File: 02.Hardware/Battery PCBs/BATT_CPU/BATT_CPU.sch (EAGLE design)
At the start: 68 parts, among them J1 2314820-6, K3 FLEX_CONN, K4 FLEX6, K5 FLEX8, U1 ATSAMD21G18_QFN, U2 TPS78230DDCR, U3 TPS78230DDCR, U4 TS3USB221A, U5 MAX9062EUK+T, U6 MAX9062EUK+T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

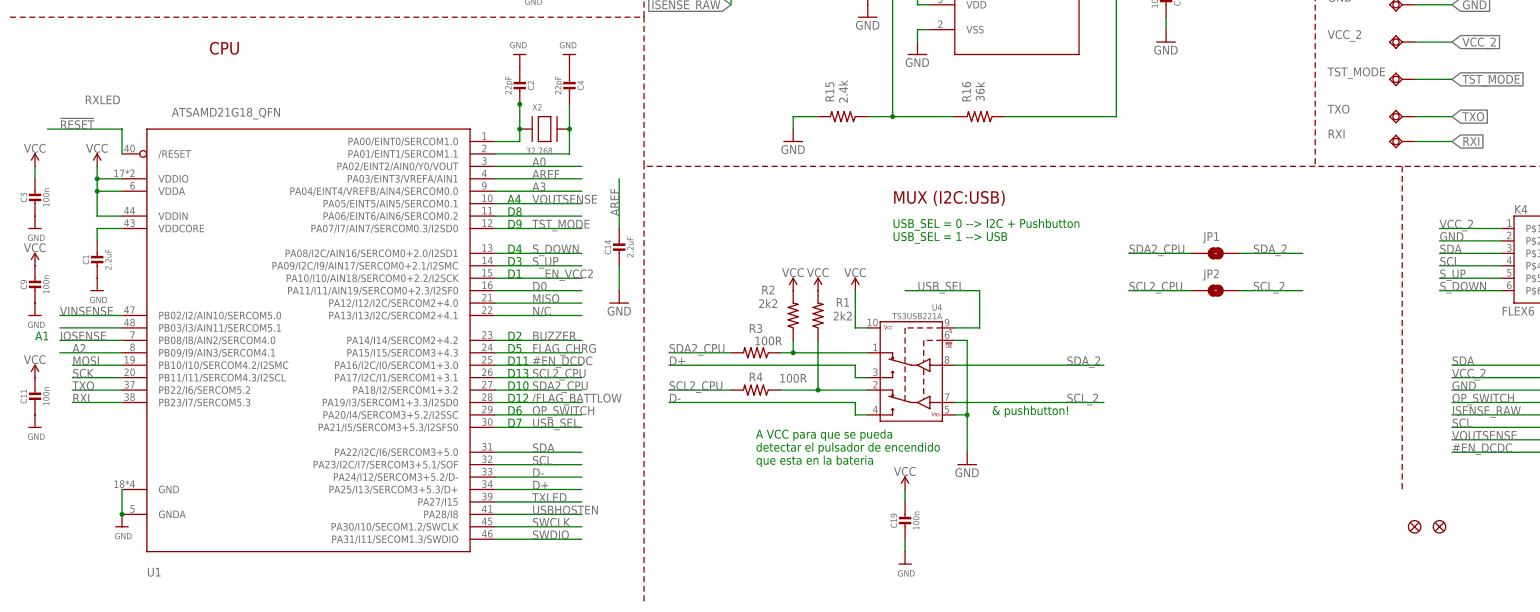
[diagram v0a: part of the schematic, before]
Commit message: Cambios revisados con David
Revision de los pcbs de la bateria.

En el DCDC se añade un diode Clamp (bat54s) en la medicion de la tension de salida.
Actualizacion de la BOM a v8.
Documentos de Cambios de versiones
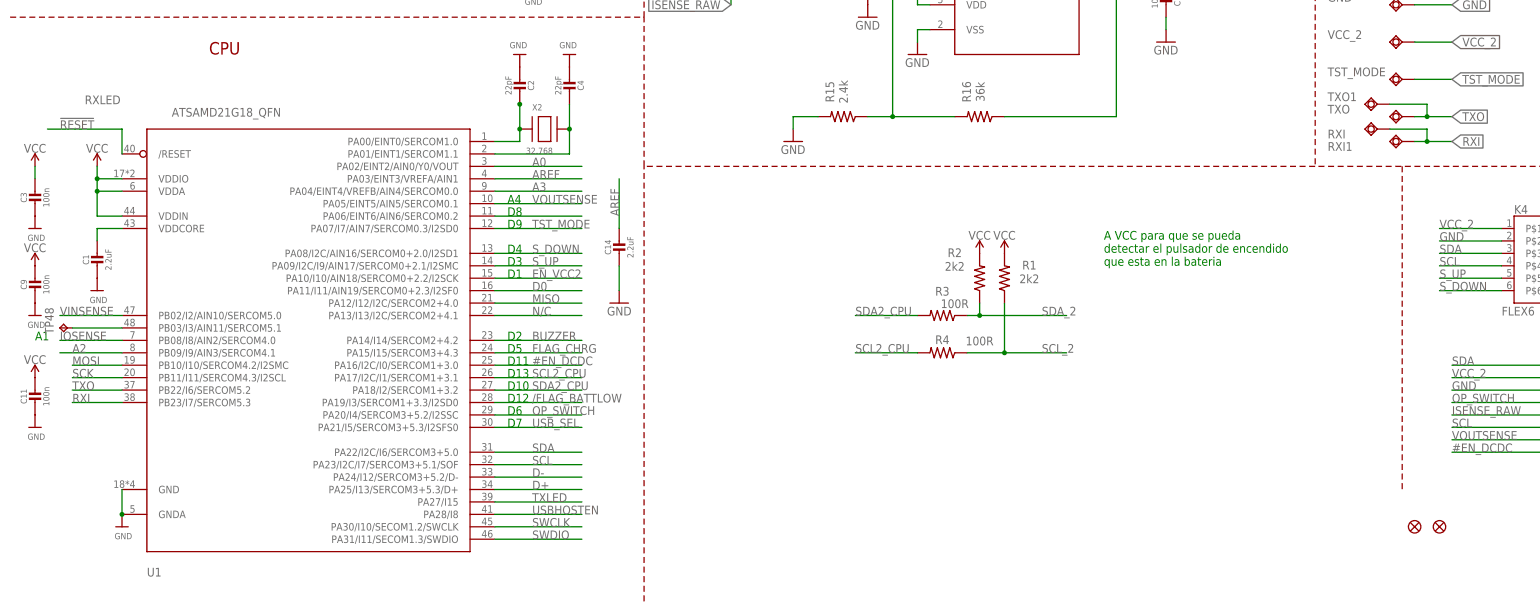
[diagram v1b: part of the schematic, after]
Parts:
- removed C19: 100n, microbuilder:CAP_CERAMIC0603_NO
- removed JP1, JP2: JUMPER-SMT_2_NO_SILK, SparkFun-Jumpers:JUMPER-SMT_2_NO_SILK
- removed U4: TS3USB221A, SparkFun-IC-Special-Function:TS3USB221A
- added RXI1, TXO1: TESTPAD_TPSQB1,27, BeagleBone_Blue_R3:TESTPAD_TPSQB1,27
- added TP48: TPTP08R, testpad:TPTP08R
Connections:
- removed net N$2: R2.1, R3.1, U4.1D+
- removed net N$3: R1.1, R4.1, U4.1D-
- net D+: no longer U4.2D+
- net D-: no longer U4.2D-
- net GND: no longer C19.2, U4.!OE, U4.VSS
- net N$15: now also TP48.TP
- net RXI: now also RXI1.TP
- net SCL2_CPU: no longer JP2.1
- net SCL_2: now also R1.1, R4.1; no longer JP2.2, U4.D-
- net SDA2_CPU: no longer JP1.1
- net SDA_2: now also R2.1, R3.1; no longer JP1.2, U4.D+
- net TXO: now also TXO1.TP
- net USB_SEL: no longer U4.S
- net VCC: no longer C19.1, U4.VCC
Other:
- note removed: "& pushbutton!"
- note removed: "MUX (I2C:USB)"
- note removed: "USB_SEL = 0 --> I2C + Pushbutton USB_SEL = 1 --> USB"
- moved on the sheet: R1, R2, R3, R4

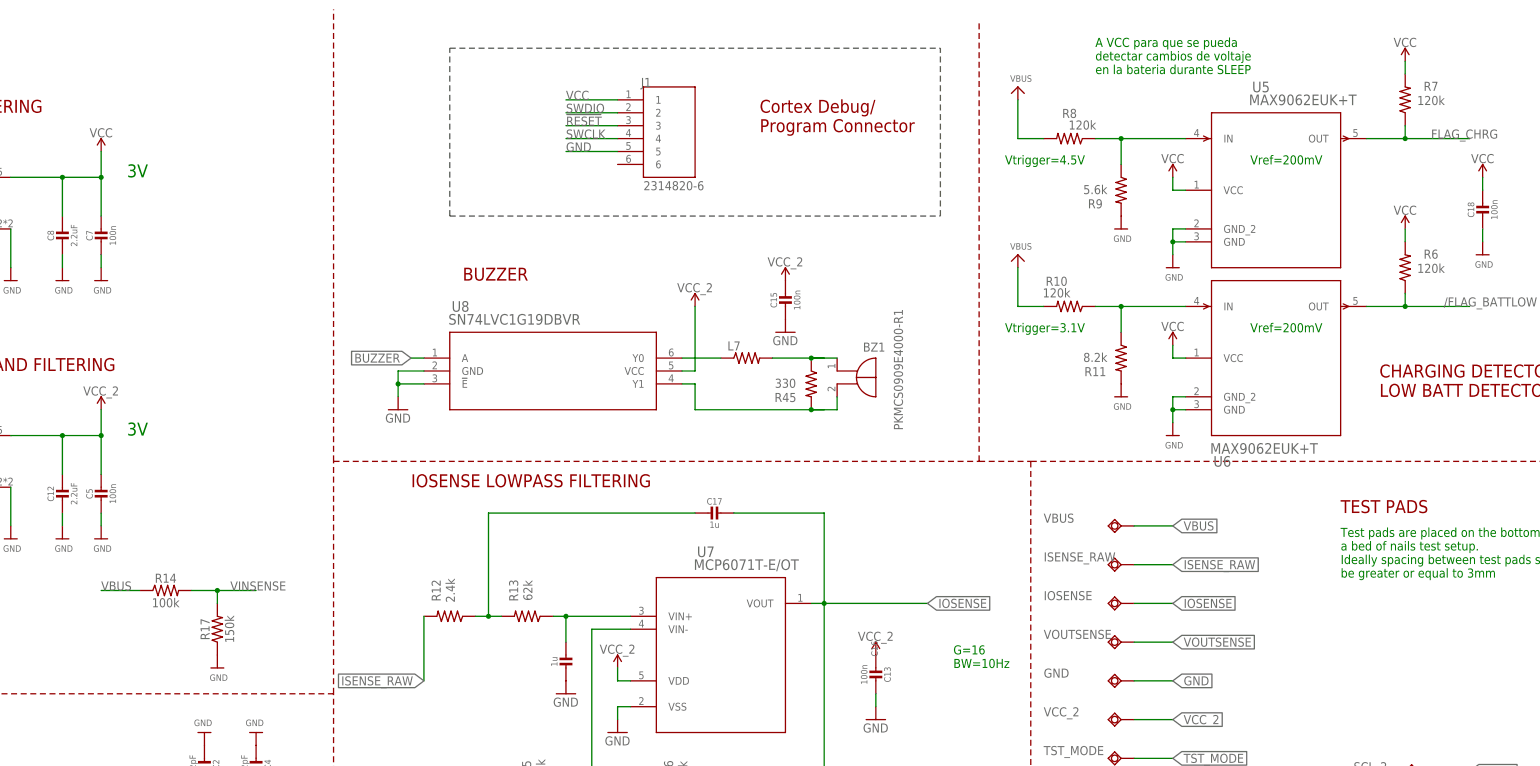
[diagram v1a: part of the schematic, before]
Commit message: Revision antes de Produccion
r6, r7: 120k a 10k
r45: no se monta
se añaden notas
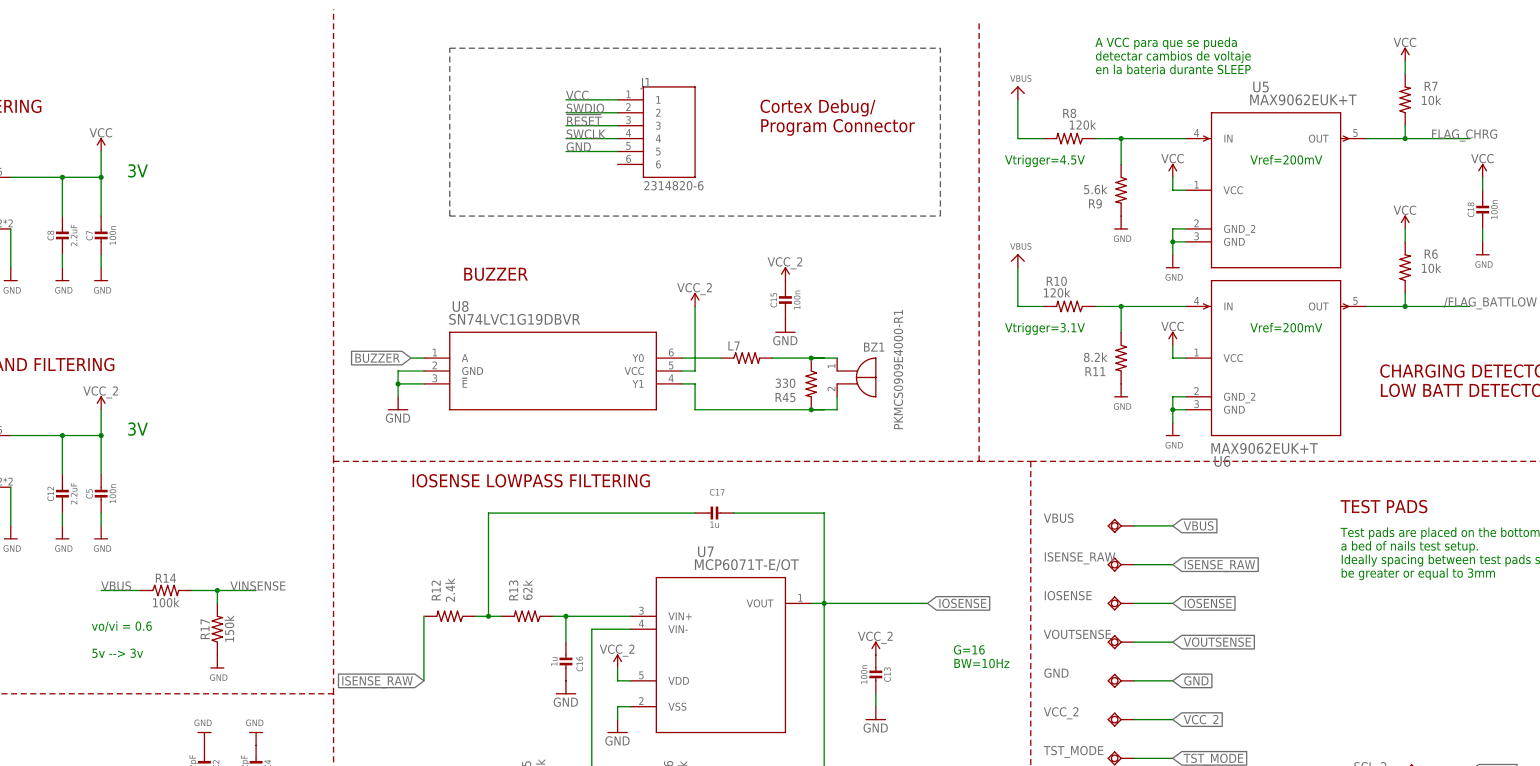
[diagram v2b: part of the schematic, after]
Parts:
- R6, R7: value 120k -> 10k
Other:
- note added: "vo/vi = 0.6 5v --> 3v"
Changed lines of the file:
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@@
 <setting verticaltext="up"/>
 </settings>
-<grid distance="0.1" unitdist="inch" unit="inch" style="lines" multiple="1" display="no" altdistance="0.01" altunitdist="inch" altunit="inch"/>
+<grid distance="1" unitdist="mm" unit="mm" style="lines" multiple="1" display="no" altdistance="0.01" altunitdist="inch" altunit="inch"/>
 <layers>
 <layer number="1" name="Top" color="4" fill="1" visible="no" active="no"/>
@@
 <part name="U5" library="MAX9062" deviceset="MAX9062EUK+T" device=""/>
 <part name="U6" library="MAX9062" deviceset="MAX9062EUK+T" device=""/>
-<part name="R6" library="SparkFun-Resistors" deviceset="RESISTOR" device="0603" value="120k"/>
-<part name="R7" library="SparkFun-Resistors" deviceset="RESISTOR" device="0603" value="120k"/>
+<part name="R6" library="SparkFun-Resistors" deviceset="RESISTOR" device="0603" value="10k"/>
+<part name="R7" library="SparkFun-Resistors" deviceset="RESISTOR" device="0603" value="10k"/>
 <part name="SUPPLY11" library="SparkFun-PowerSymbols" deviceset="VCC" device=""/>
 <part name="SUPPLY12" library="SparkFun-PowerSymbols" deviceset="VCC" device=""/>
@@
 <text x="106.68" y="81.28" size="1.778" layer="91">D8</text>
 <text x="106.68" y="78.74" size="1.778" layer="91">D9</text>
+<text x="87" y="129" size="1.778" layer="91">vo/vi = 0.6
+5v --&gt; 3v</text>
 </plain>
 <instances>
@@
 </instance>
 <instance part="C16" gate="G$1" x="180.34" y="127" smashed="yes" rot="MR0">
-<attribute name="NAME" x="241.05" y="130.79" size="1.27" layer="95" font="vector" rot="MR90" align="center"/>
+<attribute name="NAME" x="183.05" y="127.79" size="1.27" layer="95" font="vector" rot="MR90" align="center"/>
 <attribute name="VALUE" x="178.04" y="128.25" size="1.27" layer="96" font="vector" rot="MR90" align="center"/>
 </instance>
 <instance part="C17" gate="G$1" x="210.82" y="157.48" smashed="yes" rot="MR270">
-<attribute name="NAME" x="209.57" y="159.77" size="1.27" layer="95" font="vector" rot="MR0" align="center"/>
+<attribute name="NAME" x="210.11" y="161.55" size="1.27" layer="95" font="vector" rot="MR0" align="center"/>
 <attribute name="VALUE" x="209.57" y="155.18" size="1.27" layer="96" font="vector" rot="MR0" align="center"/>
 </instance>
